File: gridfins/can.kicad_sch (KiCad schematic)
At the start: 9 parts, among them U2 SN65HVD230

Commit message: feat: Massive changes, board almost ready for review
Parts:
- JP1: footprint iclr:SmallerSolderJP -> Capacitor_SMD:C_0603_1608Metric_Pad1.08x0.95mm_HandSolder

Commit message: formatting
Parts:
- JP701: renamed from JP1; now left out of the parts list
- R701: renamed from R8; value 0 -> 0Ω
- R702: renamed from R9; value 60 -> 60Ω
- R703: renamed from R10; value 60 -> 60Ω
- renumbered C15 to C701, C16 to C702, C17 to C703, D1 to D701, U2 to U701
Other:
- moved on the sheet: JP701
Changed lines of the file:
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@@
 	(wire
 		(pts
-			(xy 161.29 88.9) (xy 167.64 88.9)
+			(xy 160.02 88.9) (xy 167.64 88.9)
 		)
 		(stroke
@@
 		(pts
 			(xy 121.92 68.58) (xy 124.46 68.58)
+		)
+		(stroke
+			(width 0)
+			(type default)
+		)
+	)
+	(wire
+		(pts
+			(xy 151.13 88.9) (xy 152.4 88.9)
 		)
 		(stroke
@@
 	)
 	(label "Vref"
-		(at 153.67 88.9 180)
+		(at 151.13 88.9 180)
 		(effects
 			(font
@@
 		(dnp no)
 		(fields_autoplaced yes)
-		(property "Reference" "#PWR026"
+		(property "Reference" "#PWR0703"
 			(at 134.62 105.41 0)
 			(hide yes)
@@
 			(project "gridfins"
 				(path "/7db990e4-92e1-4f99-b4d2-435bbec1ba83/00000000-0000-0000-0000-000061942b9a"
-					(reference "#PWR026")
+					(reference "#PWR0703")
 					(unit 1)
 				)
@@
 		(dnp no)
 		(fields_autoplaced yes)
-		(property "Reference" "#PWR024"
+		(property "Reference" "#PWR0701"
 			(at 124.46 72.39 0)
 			(hide yes)
@@
 			(project "gridfins"
 				(path "/7db990e4-92e1-4f99-b4d2-435bbec1ba83/00000000-0000-0000-0000-000061942b9a"
-					(reference "#PWR024")
+					(reference "#PWR0701")
 					(unit 1)
 				)
@@
 		(dnp no)
 		(fields_autoplaced yes)
-		(property "Reference" "U2"
+		(property "Reference" "U701"
 			(at 142.24 75.1586 0)
 			(show_name no)
@@
 			(project "gridfins"
 				(path "/7db990e4-92e1-4f99-b4d2-435bbec1ba83/00000000-0000-0000-0000-000061942b9a"
-					(reference "U2")
+					(reference "U701")
 					(unit 1)
 				)
@@
 		(dnp no)
 		(fields_autoplaced yes)
-		(property "Reference" "C16"
+		(property "Reference" "C702"
 			(at 129.54 69.8562 0)
 			(show_name no)
@@
 			(project "gridfins"
 				(path "/7db990e4-92e1-4f99-b4d2-435bbec1ba83/00000000-0000-0000-0000-000061942b9a"
-					(reference "C16")
+					(reference "C702")
 					(unit 1)
 				)
@@
 		(dnp no)
 		(fields_autoplaced yes)
-		(property "Reference" "D1"
+		(property "Reference" "D701"
 			(at 190.5 87.63 90)
 			(show_name no)
@@
 			(project "gridfins"
 				(path "/7db990e4-92e1-4f99-b4d2-435bbec1ba83/00000000-0000-0000-0000-000061942b9a"
-					(reference "D1")
+					(reference "D701")
 					(unit 1)
 				)
@@
 		(dnp no)
 		(fields_autoplaced yes)
-		(property "Reference" "#PWR027"
+		(property "Reference" "#PWR0704"
 			(at 177.8 95.25 0)
 			(hide yes)
@@
 			(project "gridfins"
 				(path "/7db990e4-92e1-4f99-b4d2-435bbec1ba83/00000000-0000-0000-0000-000061942b9a"
-					(reference "#PWR027")
+					(reference "#PWR0704")
 					(unit 1)
 				)
@@
 		(dnp no)
 		(fields_autoplaced yes)
-		(property "Reference" "C15"
+		(property "Reference" "C701"
 			(at 114.3 69.85 0)
 			(show_name no)
@@
 			(project "gridfins"
 				(path "/7db990e4-92e1-4f99-b4d2-435bbec1ba83/00000000-0000-0000-0000-000061942b9a"
-					(reference "C15")
+					(reference "C701")
 					(unit 1)
 				)
@@
 		(in_pos_files yes)
 		(dnp no)
-		(property "Reference" "R8"
+		(property "Reference" "R701"
 			(at 118.11 93.98 0)
 			(show_name no)
@@
 			)
 		)
-		(property "Value" "0"
+		(property "Value" "0Ω"
 			(at 118.11 96.52 0)
 			(show_name no)
@@
 			(project "gridfins"
 				(path "/7db990e4-92e1-4f99-b4d2-435bbec1ba83/00000000-0000-0000-0000-000061942b9a"
-					(reference "R8")
+					(reference "R701")
 					(unit 1)
 				)
@@
 		(in_pos_files yes)
 		(dnp no)
-		(fields_autoplaced yes)
-		(property "Reference" "R10"
-			(at 162.56 92.71 0)
+		(property "Reference" "R703"
+			(at 161.036 92.71 0)
 			(show_name no)
 			(do_not_autoplace no)
@@
 			)
 		)
-		(property "Value" "60"
-			(at 162.56 95.25 0)
+		(property "Value" "60Ω"
+			(at 161.036 95.25 0)
 			(show_name no)
 			(do_not_autoplace no)
@@
 			(project "gridfins"
 				(path "/7db990e4-92e1-4f99-b4d2-435bbec1ba83/00000000-0000-0000-0000-000061942b9a"
-					(reference "R10")
+					(reference "R703")
 					(unit 1)
 				)
@@
 		(in_pos_files yes)
 		(dnp no)
-		(fields_autoplaced yes)
-		(property "Reference" "R9"
-			(at 162.56 82.55 0)
+		(property "Reference" "R702"
+			(at 161.036 82.55 0)
 			(show_name no)
 			(do_not_autoplace no)
@@
 			)
 		)
-		(property "Value" "60"
-			(at 162.56 85.09 0)
+		(property "Value" "60Ω"
+			(at 161.036 85.09 0)
 			(show_name no)
 			(do_not_autoplace no)
@@
 			(project "gridfins"
 				(path "/7db990e4-92e1-4f99-b4d2-435bbec1ba83/00000000-0000-0000-0000-000061942b9a"
-					(reference "R9")
+					(reference "R702")
 					(unit 1)
 				)
@@
 		(dnp no)
 		(fields_autoplaced yes)
-		(property "Reference" "C17"
+		(property "Reference" "C703"
 			(at 171.45 82.55 90)
 			(show_name no)
@@
 			(project "gridfins"
 				(path "/7db990e4-92e1-4f99-b4d2-435bbec1ba83/00000000-0000-0000-0000-000061942b9a"
-					(reference "C17")
+					(reference "C703")
 					(unit 1)
 				)
@@
 		(dnp no)
 		(fields_autoplaced yes)
-		(property "Reference" "#PWR025"
+		(property "Reference" "#PWR0702"
 			(at 124.46 80.01 0)
 			(hide yes)
@@
 			(project "gridfins"
 				(path "/7db990e4-92e1-4f99-b4d2-435bbec1ba83/00000000-0000-0000-0000-000061942b9a"
-					(reference "#PWR025")
+					(reference "#PWR0702")
 					(unit 1)
 				)
@@
 	(symbol
 		(lib_id "Jumper:SolderJumper_2_Open")
-		(at 157.48 88.9 0)
-		(unit 1)
-		(body_style 1)
-		(exclude_from_sim no)
-		(in_bom yes)
+		(at 156.21 88.9 0)
+		(unit 1)
+		(body_style 1)
+		(exclude_from_sim no)
+		(in_bom no)
 		(on_board yes)
 		(in_pos_files yes)
 		(dnp no)
 		(fields_autoplaced yes)
-		(property "Reference" "JP1"
-			(at 157.48 82.55 0)
+		(property "Reference" "JP701"
+			(at 156.21 82.55 0)
 			(show_name no)
 			(do_not_autoplace no)
@@
 		)
 		(property "Value" "TermJP"
-			(at 157.48 85.09 0)
+			(at 156.21 85.09 0)
 			(show_name no)
 			(do_not_autoplace no)
@@
 		)
 		(property "Footprint" "Capacitor_SMD:C_0603_1608Metric_Pad1.08x0.95mm_HandSolder"
-			(at 157.48 88.9 0)
+			(at 156.21 88.9 0)
 			(hide yes)
 			(show_name no)
@@
 		)
 		(property "Datasheet" ""
-			(at 157.48 88.9 0)
+			(at 156.21 88.9 0)
 			(hide yes)
 			(show_name no)
@@
 		)
 		(property "Description" "Solder Jumper, 2-pole, open"
-			(at 157.48 88.9 0)
+			(at 156.21 88.9 0)
 			(hide yes)
 			(show_name no)
@@
 			(project "gridfins"
 				(path "/7db990e4-92e1-4f99-b4d2-435bbec1ba83/00000000-0000-0000-0000-000061942b9a"
-					(reference "JP1")
-					(unit 1)
-				)
+					(reference "JP701")
+					(unit 1)
+				)

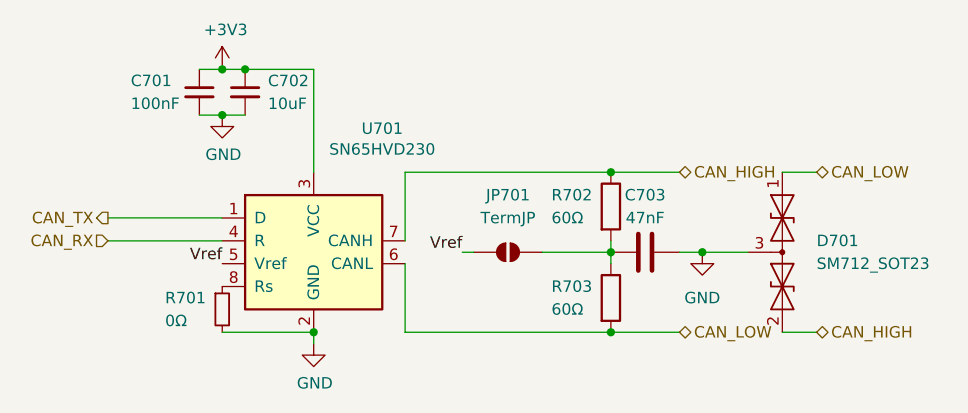
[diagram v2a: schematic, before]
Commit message: feat: Post Jack review
Changed buck inductors to be wuerth. Reduced board footprint. Incorporated review feedback
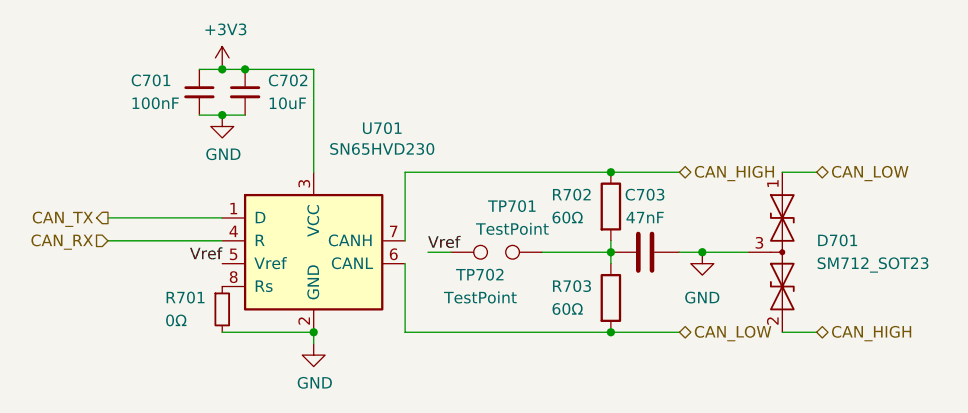
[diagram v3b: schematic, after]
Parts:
- removed JP701: TermJP, Capacitor_SMD:C_0603_1608Metric_Pad1.08x0.95mm_HandSolder, symbol Jumper:SolderJumper_2_Open
- added TP701, TP702: TestPoint, symbol Connector:TestPoint
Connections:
- net Vref: now also TP702.1
- net at C703.1, R702.2, R703.1: now also TP701.1
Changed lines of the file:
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@@
 	(wire
 		(pts
-			(xy 151.13 88.9) (xy 152.4 88.9)
+			(xy 147.32 88.9) (xy 149.86 88.9)
 		)
 		(stroke
@@
 	)
 	(label "Vref"
-		(at 151.13 88.9 180)
+		(at 147.32 88.9 0)
 		(effects
 			(font
 				(size 1.27 1.27)
 			)
-			(justify right bottom)
+			(justify left bottom)
 		)
 	)
@@
 	)
 	(symbol
+		(lib_id "Connector:TestPoint")
+		(at 149.86 88.9 270)
+		(mirror x)
+		(unit 1)
+		(body_style 1)
+		(exclude_from_sim no)
+		(in_bom yes)
+		(on_board yes)
+		(in_pos_files yes)
+		(dnp no)
+		(fields_autoplaced yes)
+		(property "Reference" "TP702"
+			(at 153.162 91.44 90)
+			(show_name no)
+			(do_not_autoplace no)
+			(effects
+				(font
+					(size 1.27 1.27)
+				)
+			)
+		)
+		(property "Value" "TestPoint"
+			(at 153.162 93.98 90)
+			(show_name no)
+			(do_not_autoplace no)
+			(effects
+				(font
+					(size 1.27 1.27)
+				)
+			)
+		)
+		(property "Footprint" ""
+			(at 149.86 83.82 0)
+			(hide yes)
+			(show_name no)
+			(do_not_autoplace no)
+			(effects
+				(font
+					(size 1.27 1.27)
+				)
+			)
+		)
+		(property "Datasheet" ""
+			(at 149.86 83.82 0)
+			(hide yes)
+			(show_name no)
+			(do_not_autoplace no)
+			(effects
+				(font
+					(size 1.27 1.27)
+				)
+			)
+		)
+		(property "Description" "test point"
+			(at 149.86 88.9 0)
+			(hide yes)
+			(show_name no)
+			(do_not_autoplace no)
+			(effects
+				(font
+					(size 1.27 1.27)
+				)
+			)
+		)
+		(pin "1"
+		)
+		(instances
+			(project "gridfins"
+				(path "/7db990e4-92e1-4f99-b4d2-435bbec1ba83/00000000-0000-0000-0000-000061942b9a"
+					(reference "TP702")
+					(unit 1)
+				)
+			)
+		)
+	)
+	(symbol
 		(lib_id "Diode:SM712_SOT23")
 		(at 186.69 88.9 270)
@@
 	)
 	(symbol
+		(lib_id "Connector:TestPoint")
+		(at 160.02 88.9 90)
+		(unit 1)
+		(body_style 1)
+		(exclude_from_sim no)
+		(in_bom yes)
+		(on_board yes)
+		(in_pos_files yes)
+		(dnp no)
+		(fields_autoplaced yes)
+		(property "Reference" "TP701"
+			(at 156.718 83.82 90)
+			(show_name no)
+			(do_not_autoplace no)
+			(effects
+				(font
+					(size 1.27 1.27)
+				)
+			)
+		)
+		(property "Value" "TestPoint"
+			(at 156.718 86.36 90)
+			(show_name no)
+			(do_not_autoplace no)
+			(effects
+				(font
+					(size 1.27 1.27)
+				)
+			)
+		)
+		(property "Footprint" ""
+			(at 160.02 83.82 0)
+			(hide yes)
+			(show_name no)
+			(do_not_autoplace no)
+			(effects
+				(font
+					(size 1.27 1.27)
+				)
+			)
+		)
+		(property "Datasheet" ""
+			(at 160.02 83.82 0)
+			(hide yes)
+			(show_name no)
+			(do_not_autoplace no)
+			(effects
+				(font
+					(size 1.27 1.27)
+				)
+			)
+		)
+		(property "Description" "test point"
+			(at 160.02 88.9 0)
+			(hide yes)
+			(show_name no)
+			(do_not_autoplace no)
+			(effects
+				(font
+					(size 1.27 1.27)
+				)
+			)
+		)
+		(pin "1"
+		)
+		(instances
+			(project "gridfins"
+				(path "/7db990e4-92e1-4f99-b4d2-435bbec1ba83/00000000-0000-0000-0000-000061942b9a"
+					(reference "TP701")
+					(unit 1)
+				)
+			)
+		)
+	)
+	(symbol
 		(lib_id "Device:C_Small")
 		(at 121.92 71.12 0)
@@
 					(unit 1)
 				)
-			)
-		)
-	)
-	(symbol
-		(lib_id "Jumper:SolderJumper_2_Open")
-		(at 156.21 88.9 0)
-		(unit 1)
-		(body_style 1)
-		(exclude_from_sim no)
-		(in_bom no)
-		(on_board yes)
-		(in_pos_files yes)
-		(dnp no)
-		(fields_autoplaced yes)
-		(property "Reference" "JP701"
-			(at 156.21 82.55 0)
-			(show_name no)
-			(do_not_autoplace no)
-			(effects
-				(font
-					(size 1.27 1.27)
-				)
-			)
-		)
-		(property "Value" "TermJP"
-			(at 156.21 85.09 0)
-			(show_name no)
-			(do_not_autoplace no)
-			(effects
-				(font
-					(size 1.27 1.27)
-				)
-			)
-		)
-		(property "Footprint" "Capacitor_SMD:C_0603_1608Metric_Pad1.08x0.95mm_HandSolder"
-			(at 156.21 88.9 0)
-			(hide yes)
-			(show_name no)
-			(do_not_autoplace no)
-			(effects
-				(font
-					(size 1.27 1.27)
-				)
-			)
-		)
-		(property "Datasheet" ""
-			(at 156.21 88.9 0)
-			(hide yes)
-			(show_name no)
-			(do_not_autoplace no)
-			(effects
-				(font
-					(size 1.27 1.27)
-				)
-			)
-		)
-		(property "Description" "Solder Jumper, 2-pole, open"
-			(at 156.21 88.9 0)
-			(hide yes)
-			(show_name no)
-			(do_not_autoplace no)
-			(effects
-				(font
-					(size 1.27 1.27)
-				)
-			)
-		)
-		(pin "1"
-		)
-		(pin "2"
-		)
-		(instances
-			(project "gridfins"
-				(path "/7db990e4-92e1-4f99-b4d2-435bbec1ba83/00000000-0000-0000-0000-000061942b9a"
-					(reference "JP701")
-					(unit 1)
-				)
